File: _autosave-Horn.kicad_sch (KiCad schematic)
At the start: 8 parts, among them U1 AP62300TWU

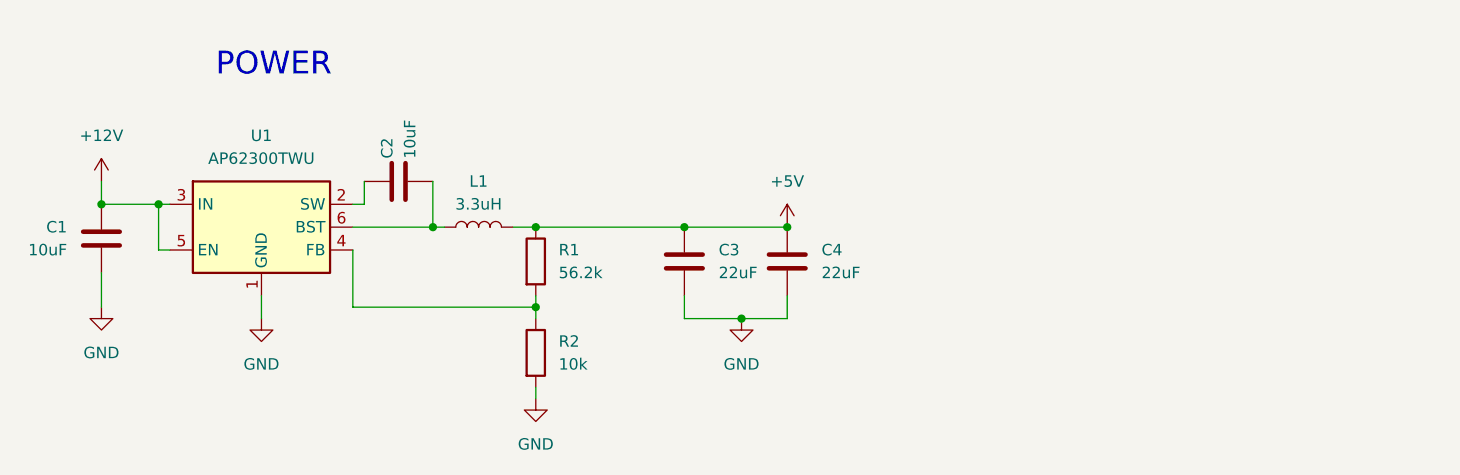
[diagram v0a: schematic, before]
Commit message: Added LDO
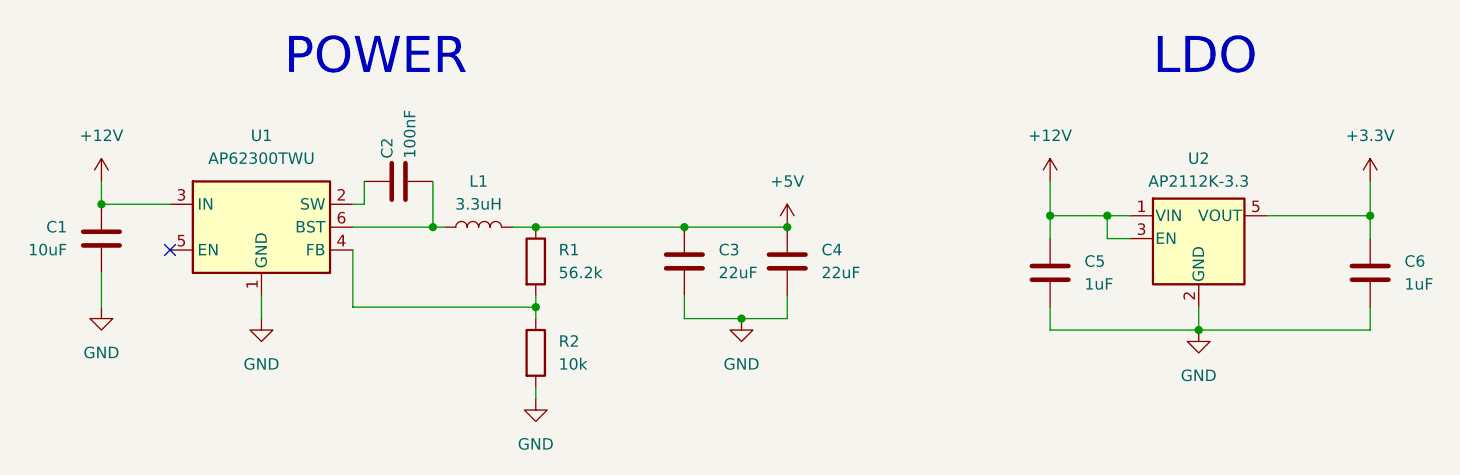
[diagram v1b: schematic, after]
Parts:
- added C5, C6: 1uF, symbol Device:C
- added U2: AP2112K-3.3, Package_TO_SOT_SMD:SOT-23-5, symbol Regulator_Linear:AP2112K-3.3
- C2: value 10uF -> 100nF
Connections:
- net +12V: now also C5.1, U2.1 (VIN), U2.3 (EN); no longer U1.5 (EN)
- net GND: now also C5.2, C6.2, U2.2 (GND)
- new net +3.3V: C6.1, U2.5 (VOUT)
- no-connect marks 0 -> 1
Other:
- note added: "LDO"
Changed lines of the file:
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@@
   (junction (at 113.03 52.07) (diameter 0) (color 0 0 0 0)
   )
-  (junction (at 48.26 39.37) (diameter 0) (color 0 0 0 0)
+  (junction (at 153.67 40.64) (diameter 0) (color 0 0 0 0)
   )
   (junction (at 41.91 39.37) (diameter 0) (color 0 0 0 0)
   )
+  (junction (at 163.83 53.34) (diameter 0) (color 0 0 0 0)
+  )
   (junction (at 106.68 41.91) (diameter 0) (color 0 0 0 0)
   )
+  (junction (at 182.88 40.64) (diameter 0) (color 0 0 0 0)
+  )
+  (junction (at 147.32 40.64) (diameter 0) (color 0 0 0 0)
+  )
   (junction (at 90.17 41.91) (diameter 0) (color 0 0 0 0)
   )
@@
   (junction (at 90.17 50.8) (diameter 0) (color 0 0 0 0)
   )
-  (wire (pts (xy 48.26 39.37) (xy 49.53 39.37))
-    (stroke (width 0) (type default))
-  )
-  (wire (pts (xy 41.91 39.37) (xy 48.26 39.37))
+  (no_connect (at 49.53 44.45))
+  (wire (pts (xy 182.88 40.64) (xy 182.88 43.18))
+    (stroke (width 0) (type default))
+  )
+  (wire (pts (xy 41.91 39.37) (xy 49.53 39.37))
     (stroke (width 0) (type default))
   )
@@
     (stroke (width 0) (type default))
   )
+  (wire (pts (xy 163.83 50.8) (xy 163.83 53.34))
+    (stroke (width 0) (type default))
+  )
+  (wire (pts (xy 182.88 40.64) (xy 182.88 36.83))
+    (stroke (width 0) (type default))
+  )
   (wire (pts (xy 90.17 50.8) (xy 69.85 50.8))
     (stroke (width 0) (type default))
   )
+  (wire (pts (xy 153.67 40.64) (xy 156.21 40.64))
+    (stroke (width 0) (type default))
+  )
   (wire (pts (xy 90.17 49.53) (xy 90.17 50.8))
     (stroke (width 0) (type default))
@@
     (stroke (width 0) (type default))
   )
+  (wire (pts (xy 147.32 40.64) (xy 147.32 43.18))
+    (stroke (width 0) (type default))
+  )
+  (wire (pts (xy 153.67 43.18) (xy 156.21 43.18))
+    (stroke (width 0) (type default))
+  )
   (wire (pts (xy 69.85 39.37) (xy 71.12 39.37))
     (stroke (width 0) (type default))
@@
     (stroke (width 0) (type default))
   )
+  (wire (pts (xy 182.88 50.8) (xy 182.88 53.34))
+    (stroke (width 0) (type default))
+  )
   (wire (pts (xy 90.17 50.8) (xy 90.17 52.07))
     (stroke (width 0) (type default))
@@
     (stroke (width 0) (type default))
   )
+  (wire (pts (xy 147.32 36.83) (xy 147.32 40.64))
+    (stroke (width 0) (type default))
+  )
   (wire (pts (xy 90.17 41.91) (xy 106.68 41.91))
     (stroke (width 0) (type default))
@@
     (stroke (width 0) (type default))
   )
+  (wire (pts (xy 182.88 53.34) (xy 163.83 53.34))
+    (stroke (width 0) (type default))
+  )
   (wire (pts (xy 59.69 49.53) (xy 59.69 52.07))
     (stroke (width 0) (type default))
   )
+  (wire (pts (xy 171.45 40.64) (xy 182.88 40.64))
+    (stroke (width 0) (type default))
+  )
   (wire (pts (xy 41.91 46.99) (xy 41.91 50.8))
     (stroke (width 0) (type default))
   )
-  (wire (pts (xy 48.26 44.45) (xy 48.26 39.37))
+  (wire (pts (xy 147.32 40.64) (xy 153.67 40.64))
     (stroke (width 0) (type default))
   )
@@
     (stroke (width 0) (type default))
   )
+  (wire (pts (xy 147.32 50.8) (xy 147.32 53.34))
+    (stroke (width 0) (type default))
+  )
+  (wire (pts (xy 147.32 53.34) (xy 163.83 53.34))
+    (stroke (width 0) (type default))
+  )
   (wire (pts (xy 106.68 52.07) (xy 113.03 52.07))
     (stroke (width 0) (type default))
   )
+  (wire (pts (xy 153.67 40.64) (xy 153.67 43.18))
+    (stroke (width 0) (type default))
+  )
   (wire (pts (xy 78.74 41.91) (xy 80.01 41.91))
     (stroke (width 0) (type default))
@@
     (stroke (width 0) (type default))
   )
-  (wire (pts (xy 49.53 44.45) (xy 48.26 44.45))
-    (stroke (width 0) (type default))
-  )
   (wire (pts (xy 118.11 49.53) (xy 118.11 52.07))
     (stroke (width 0) (type default))
   )
-  (text "POWER" (at 54.61 25.4 0)
-    (effects (font (size 2.54 2.54)) (justify left bottom))
+  (text "POWER" (at 62.23 25.4 0)
+    (effects (font (size 4 4)) (justify left bottom))
+  )
+  (text "LDO" (at 158.75 25.4 0)
+    (effects (font (size 4 4)) (justify left bottom))
   )
   (symbol (lib_id "power:GND") (at 90.17 60.96 0) (unit 1)
@@
         (path "/db95c586-8bdb-4fed-be35-89b6ade80a28"
           (reference "#PWR04") (unit 1)
+        )
+      )
+    )
+  )
+  (symbol (lib_id "Regulator_Linear:AP2112K-3.3") (at 163.83 43.18 0) (unit 1)
+    (in_bom yes) (on_board yes) (dnp no) (fields_autoplaced)
+    (property "Reference" "U2" (at 163.83 34.29 0)
+      (effects (font (size 1.27 1.27)))
+    )
+    (property "Value" "AP2112K-3.3" (at 163.83 36.83 0)
+      (effects (font (size 1.27 1.27)))
+    )
+    (property "Footprint" "Package_TO_SOT_SMD:SOT-23-5" (at 163.83 34.925 0)
+      (effects (font (size 1.27 1.27)) hide)
+    )
+    (property "Datasheet" "https://www.diodes.com/assets/Datasheets/AP2112.pdf" (at 163.83 40.64 0)
+      (effects (font (size 1.27 1.27)) hide)
+    )
+    (pin "5")
+    (pin "4")
+    (pin "1")
+    (pin "2")
+    (pin "3")
+    (instances
+      (project "Horn"
+        (path "/db95c586-8bdb-4fed-be35-89b6ade80a28"
+          (reference "U2") (unit 1)
         )
       )
@@
     )
   )
+  (symbol (lib_id "power:+3.3V") (at 182.88 36.83 0) (unit 1)
+    (in_bom yes) (on_board yes) (dnp no) (fields_autoplaced)
+    (property "Reference" "#PWR08" (at 182.88 40.64 0)
+      (effects (font (size 1.27 1.27)) hide)
+    )
+    (property "Value" "+3.3V" (at 182.88 31.75 0)
+      (effects (font (size 1.27 1.27)))
+    )
+    (property "Footprint" "" (at 182.88 36.83 0)
+      (effects (font (size 1.27 1.27)) hide)
+    )
+    (property "Datasheet" "" (at 182.88 36.83 0)
+      (effects (font (size 1.27 1.27)) hide)
+    )
+    (pin "1")
+    (instances
+      (project "Horn"
+        (path "/db95c586-8bdb-4fed-be35-89b6ade80a28"
+          (reference "#PWR08") (unit 1)
+        )
+      )
+    )
+  )
   (symbol (lib_id "power:GND") (at 113.03 52.07 0) (unit 1)
     (in_bom yes) (on_board yes) (dnp no) (fields_autoplaced)
@@
         (path "/db95c586-8bdb-4fed-be35-89b6ade80a28"
           (reference "R1") (unit 1)
+        )
+      )
+    )
+  )
+  (symbol (lib_id "power:+12V") (at 147.32 36.83 0) (unit 1)
+    (in_bom yes) (on_board yes) (dnp no) (fields_autoplaced)
+    (property "Reference" "#PWR07" (at 147.32 40.64 0)
+      (effects (font (size 1.27 1.27)) hide)
+    )
+    (property "Value" "+12V" (at 147.32 31.75 0)
+      (effects (font (size 1.27 1.27)))
+    )
+    (property "Footprint" "" (at 147.32 36.83 0)
+      (effects (font (size 1.27 1.27)) hide)
+    )
+    (property "Datasheet" "" (at 147.32 36.83 0)
+      (effects (font (size 1.27 1.27)) hide)
+    )
+    (pin "1")
+    (instances
+      (project "Horn"
+        (path "/db95c586-8bdb-4fed-be35-89b6ade80a28"
+          (reference "#PWR07") (unit 1)
         )
       )
@@
     )
   )
+  (symbol (lib_id "power:GND") (at 163.83 53.34 0) (unit 1)
+    (in_bom yes) (on_board yes) (dnp no) (fields_autoplaced)
+    (property "Reference" "#PWR09" (at 163.83 59.69 0)
+      (effects (font (size 1.27 1.27)) hide)
+    )
+    (property "Value" "GND" (at 163.83 58.42 0)
+      (effects (font (size 1.27 1.27)))
+    )
+    (property "Footprint" "" (at 163.83 53.34 0)
+      (effects (font (size 1.27 1.27)) hide)
+    )
+    (property "Datasheet" "" (at 163.83 53.34 0)
+      (effects (font (size 1.27 1.27)) hide)
+    )
+    (pin "1")
+    (instances
+      (project "Horn"
+        (path "/db95c586-8bdb-4fed-be35-89b6ade80a28"
+          (reference "#PWR09") (unit 1)
+        )
+      )
+    )
+  )
+  (symbol (lib_id "Device:C") (at 182.88 46.99 0) (unit 1)
+    (in_bom yes) (on_board yes) (dnp no)
+    (property "Reference" "C6" (at 186.69 45.72 0)
+      (effects (font (size 1.27 1.27)) (justify left))
+    )
+    (property "Value" "1uF" (at 186.69 48.26 0)
+      (effects (font (size 1.27 1.27)) (justify left))
+    )
+    (property "Footprint" "" (at 183.8452 50.8 0)
+      (effects (font (size 1.27 1.27)) hide)
+    )
+    (property "Datasheet" "~" (at 182.88 46.99 0)
+      (effects (font (size 1.27 1.27)) hide)
+    )
+    (pin "1")
+    (pin "2")
+    (instances
+      (project "Horn"
+        (path "/db95c586-8bdb-4fed-be35-89b6ade80a28"
+          (reference "C6") (unit 1)
+        )
+      )
+    )
+  )
+  (symbol (lib_id "Device:C") (at 147.32 46.99 0) (unit 1)
+    (in_bom yes) (on_board yes) (dnp no)
+    (property "Reference" "C5" (at 151.13 45.72 0)
+      (effects (font (size 1.27 1.27)) (justify left))
+    )
+    (property "Value" "1uF" (at 151.13 48.26 0)
+      (effects (font (size 1.27 1.27)) (justify left))
+    )
+    (property "Footprint" "" (at 148.2852 50.8 0)
+      (effects (font (size 1.27 1.27)) hide)
+    )
+    (property "Datasheet" "~" (at 147.32 46.99 0)
+      (effects (font (size 1.27 1.27)) hide)
+    )
+    (pin "1")
+    (pin "2")
+    (instances
+      (project "Horn"
+        (path "/db95c586-8bdb-4fed-be35-89b6ade80a28"
+          (reference "C5") (unit 1)
+        )
+      )
+    )
+  )
   (symbol (lib_id "power:+12V") (at 41.91 36.83 0) (unit 1)
     (in_bom yes) (on_board yes) (dnp no) (fields_autoplaced)
@@
       (effects (font (size 1.27 1.27)) (justify left))
     )
-    (property "Value" "10uF" (at 76.2 34.29 0)
-      (effects (font (size 1.27 1.27)) (justify left))
-    )
+    (property "Value" "100nF" (at 76.2 34.29 0)
+      (effects (font (size 1.27 1.27)) (justify left))
+    )
